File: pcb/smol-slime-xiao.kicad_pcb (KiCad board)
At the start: 4 copper layers, 20 x 23.5 mm, 11 parts, among them J2 Conn_01x02, U1 ICM-45686, U3 1532H, U4 XIAO-nRF52840-SMD

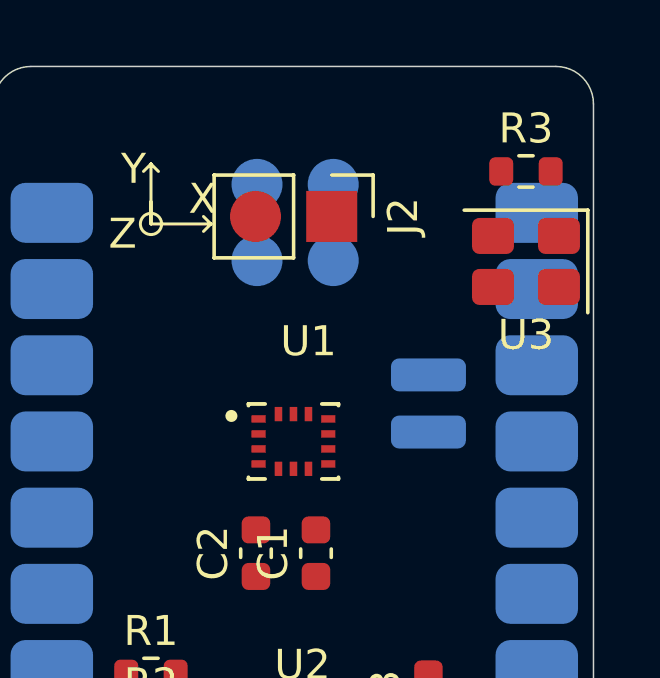
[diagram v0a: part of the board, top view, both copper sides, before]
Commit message: Add battery JST connector
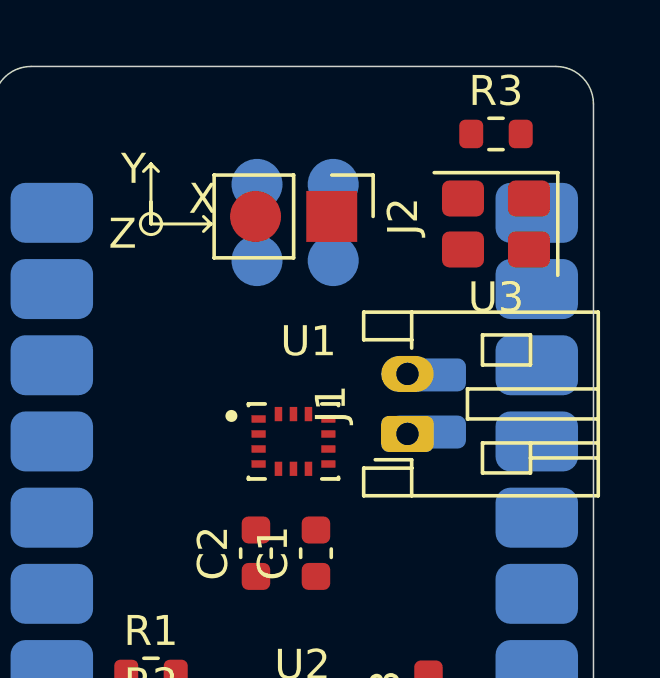
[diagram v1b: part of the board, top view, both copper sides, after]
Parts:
- added J1: Conn_01x02, Connector_JST:JST_PH_S2B-PH-K_1x02_P2.00mm_Horizontal, F.Cu at (153.8, 99.8)
- moved R3 1.60 mm to (156.8, 89.8)
- moved U3 1.60 mm to (156.8, 92.8)
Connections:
- J2 pad 1: GND -> +5V
- J2 pad 2: +5V -> GND

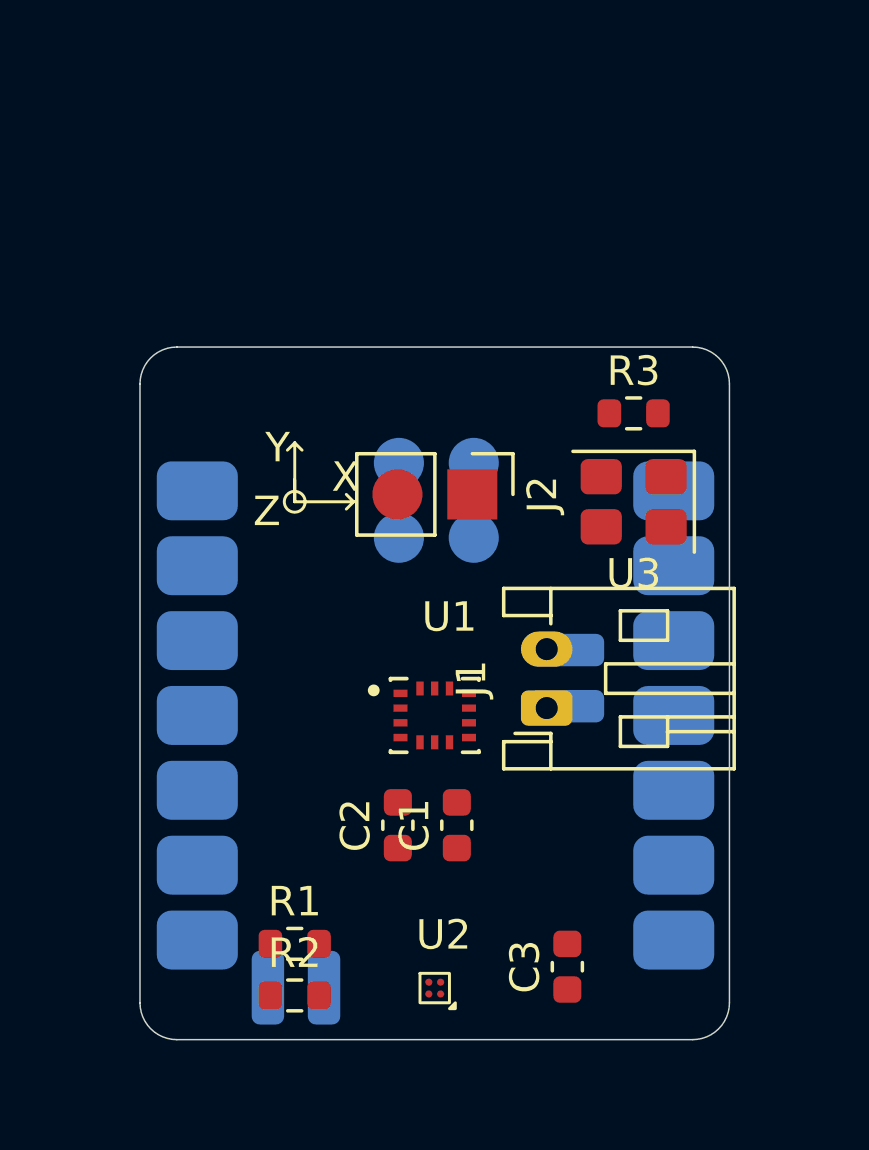
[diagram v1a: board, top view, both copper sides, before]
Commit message: Add descriptions to silkscreen
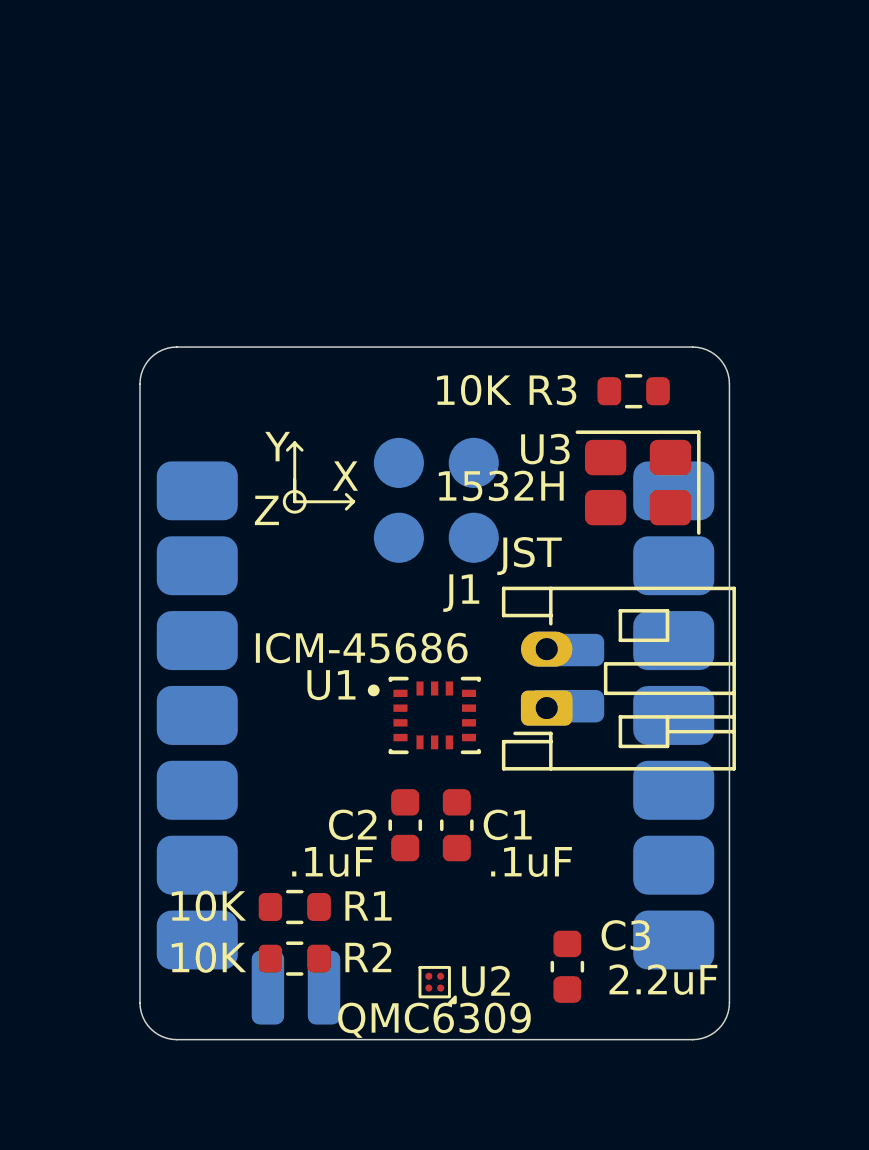
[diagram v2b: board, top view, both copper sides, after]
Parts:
- removed J2: Conn_01x02, Generic:PinPads_1x02_P2.54mm
- C1, C2: value 0.1uF -> .1uF
- J1: value Conn_01x02 -> JST
- U2: value ~ -> QMC6309
- moved R1 1.25 mm to (145.2, 106.5)
- moved R2 1.25 mm to (145.2, 108.2)
- moved R3 0.75 mm to (156.8, 89.0)
- moved U3 0.67 mm to (156.9, 92.1)
- moved C2 0.25 mm to (149.0, 103.7)
- moved U2 0.20 mm to (150.0, 109.0)

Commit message: Update pin pad footprint
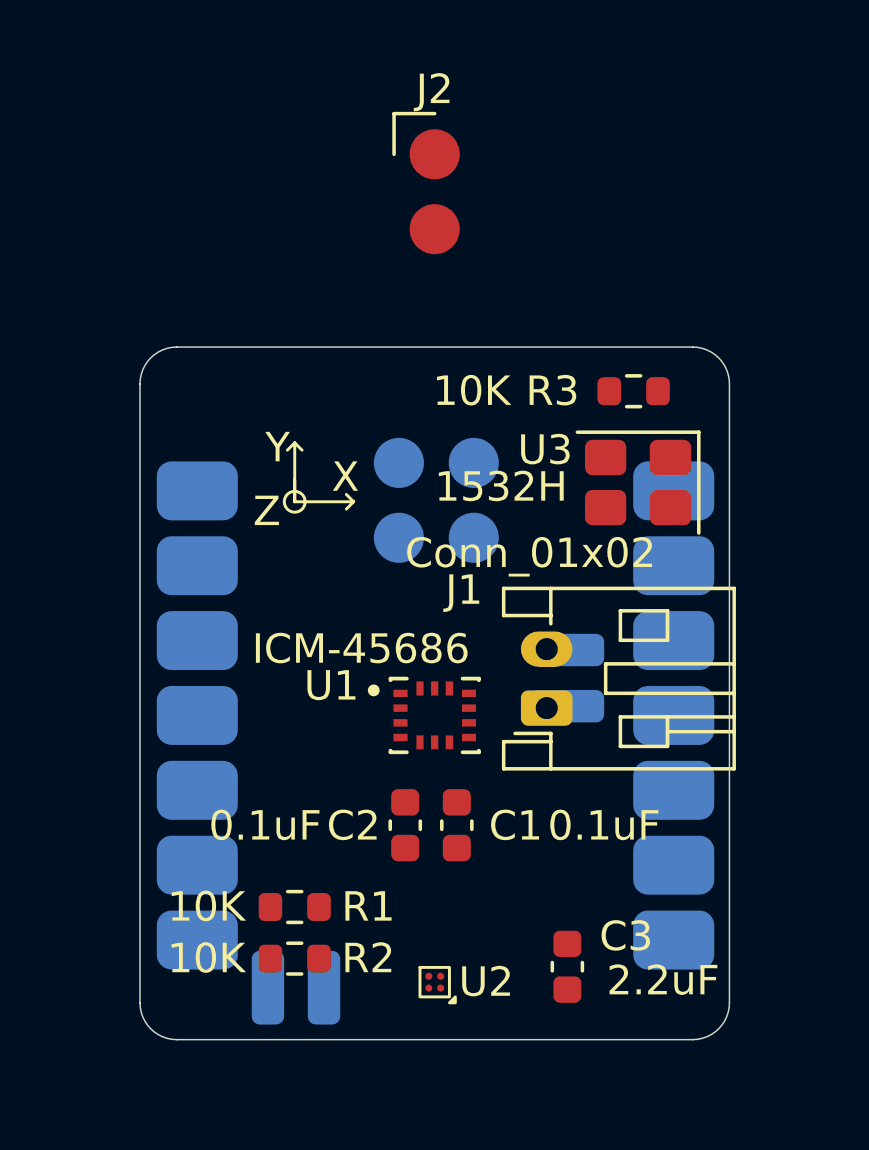
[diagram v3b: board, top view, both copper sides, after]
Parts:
- added J2: Conn_01x02, Generic:PinPads_1x02_P2.54mm, F.Cu at (150.0, 81.0)
- C1, C2: value .1uF -> 0.1uF
- J1: value JST -> Conn_01x02
- U2: value QMC6309 -> ~
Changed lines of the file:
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@@
 			)
 		)
-		(property "Value" "JST"
+		(property "Value" "Conn_01x02"
 			(at 5.25 -0.55 180)
 			(layer "F.SilkS")
@@
 			)
 		)
-		(property "Value" "QMC6309"
+		(property "Value" "~"
 			(at 0 1.25 0)
 			(unlocked yes)
@@
 		(tags "capacitor")
 		(property "Reference" "C1"
-			(at -0.025 1.75 180)
-			(layer "F.SilkS")
-			(effects
-				(font
-					(size 1 1)
-					(thickness 0.15)
-				)
-			)
-		)
-		(property "Value" ".1uF"
-			(at -1.275 2.5 180)
+			(at -0.025 2 180)
+			(layer "F.SilkS")
+			(effects
+				(font
+					(size 1 1)
+					(thickness 0.15)
+				)
+			)
+		)
+		(property "Value" "0.1uF"
+			(at -0.025 5 180)
 			(layer "F.SilkS")
 			(effects
@@
 			)
 		)
+	)
+	(footprint "Generic:PinPads_1x02_P2.54mm"
+		(layer "F.Cu")
+		(at 150 80.96)
+		(descr "Through hole straight pin header, 1x02, 2.54mm pitch, single row")
+		(tags "Through hole pin header THT 1x02 2.54mm single row")
+		(property "Reference" "J2"
+			(at 0 -2.2 0)
+			(layer "F.SilkS")
+			(effects
+				(font
+					(size 1 1)
+					(thickness 0.15)
+				)
+			)
+		)
+		(property "Value" "Conn_01x02"
+			(at 0 4.92 0)
+			(layer "F.Fab")
+			(hide yes)
+			(effects
+				(font
+					(size 1 1)
+					(thickness 0.15)
+				)
+			)
+		)
+		(property "Datasheet" "~"
+			(at 0 0 0)
+			(layer "F.Fab")
+			(hide yes)
+			(effects
+				(font
+					(size 1.27 1.27)
+					(thickness 0.15)
+				)
+			)
+		)
+		(property "Description" "Generic connector, single row, 01x02, script generated (kicad-library-utils/schlib/autogen/connector/)"
+			(at 0 0 0)
+			(layer "F.Fab")
+			(hide yes)
+			(effects
+				(font
+					(size 1.27 1.27)
+					(thickness 0.15)
+				)
+			)
+		)
+		(property ki_fp_filters "Connector*:*_1x??_*")
+		(sheetname "/")
+		(sheetfile "smol-slime-xiao.kicad_sch")
+		(attr through_hole)
+		(fp_line
+			(start -1.38 -1.38)
+			(end 0 -1.38)
+			(stroke
+				(width 0.12)
+				(type solid)
+			)
+			(layer "F.SilkS")
+		)
+		(fp_line
+			(start -1.38 0)
+			(end -1.38 -1.38)
+			(stroke
+				(width 0.12)
+				(type solid)
+			)
+			(layer "F.SilkS")
+		)
+		(fp_line
+			(start -1.5 -1.5)
+			(end -1.5 4)
+			(stroke
+				(width 0.05)
+				(type solid)
+			)
+			(layer "F.CrtYd")
+		)
+		(fp_line
+			(start -1.5 4)
+			(end 1.5 4)
+			(stroke
+				(width 0.05)
+				(type solid)
+			)
+			(layer "F.CrtYd")
+		)
+		(fp_line
+			(start 1.5 -1.5)
+			(end -1.5 -1.5)
+			(stroke
+				(width 0.05)
+				(type solid)
+			)
+			(layer "F.CrtYd")
+		)
+		(fp_line
+			(start 1.5 4)
+			(end 1.5 -1.5)
+			(stroke
+				(width 0.05)
+				(type solid)
+			)
+			(layer "F.CrtYd")
+		)
+		(fp_line
+			(start -1.27 -0.635)
+			(end -0.635 -1.27)
+			(stroke
+				(width 0.1)
+				(type solid)
+			)
+			(layer "F.Fab")
+		)
+		(fp_line
+			(start -1.27 3.81)
+			(end -1.27 -0.635)
+			(stroke
+				(width 0.1)
+				(type solid)
+			)
+			(layer "F.Fab")
+		)
+		(fp_line
+			(start -0.635 -1.27)
+			(end 1.27 -1.27)
+			(stroke
+				(width 0.1)
+				(type solid)
+			)
+			(layer "F.Fab")
+		)
+		(fp_line
+			(start 1.27 -1.27)
+			(end 1.27 3.81)
+			(stroke
+				(width 0.1)
+				(type solid)
+			)
+			(layer "F.Fab")
+		)
+		(fp_line
+			(start 1.27 3.81)
+			(end -1.27 3.81)
+			(stroke
+				(width 0.1)
+				(type solid)
+			)
+			(layer "F.Fab")
+		)
+		(fp_text user "${REFERENCE}"
+			(at 3 1.27 90)
+			(layer "F.Fab")
+			(effects
+				(font
+					(size 1 1)
+					(thickness 0.15)
+				)
+			)
+		)
+		(pad "1" smd circle
+			(at 0 0)
+			(size 1.7 1.7)
+			(layers "F.Cu" "F.Mask" "F.Paste")
+			(net 18 "+5V")
+			(pinfunction "Pin_1")
+			(pintype "passive")
+		)
+		(pad "2" smd circle
+			(at 0 2.54)
+			(size 1.7 1.7)
+			(layers "F.Cu" "F.Mask" "F.Paste")
+			(net 1 "GND")
+			(pinfunction "Pin_2")
+			(pintype "passive")
+		)
+		(embedded_fonts no)
 	)
 	(footprint "Capacitor_SMD:C_0603_1608Metric"
@@
 			)
 		)
-		(property "Value" ".1uF"
-			(at -1.275 -2.5 180)
-			(layer "F.SilkS")
-			(effects
+		(property "Value" "0.1uF"
+			(at -0.025 -4.75 180)
+			(layer "F.SilkS")
+			(effects

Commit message: Revert silkscreen verbosity
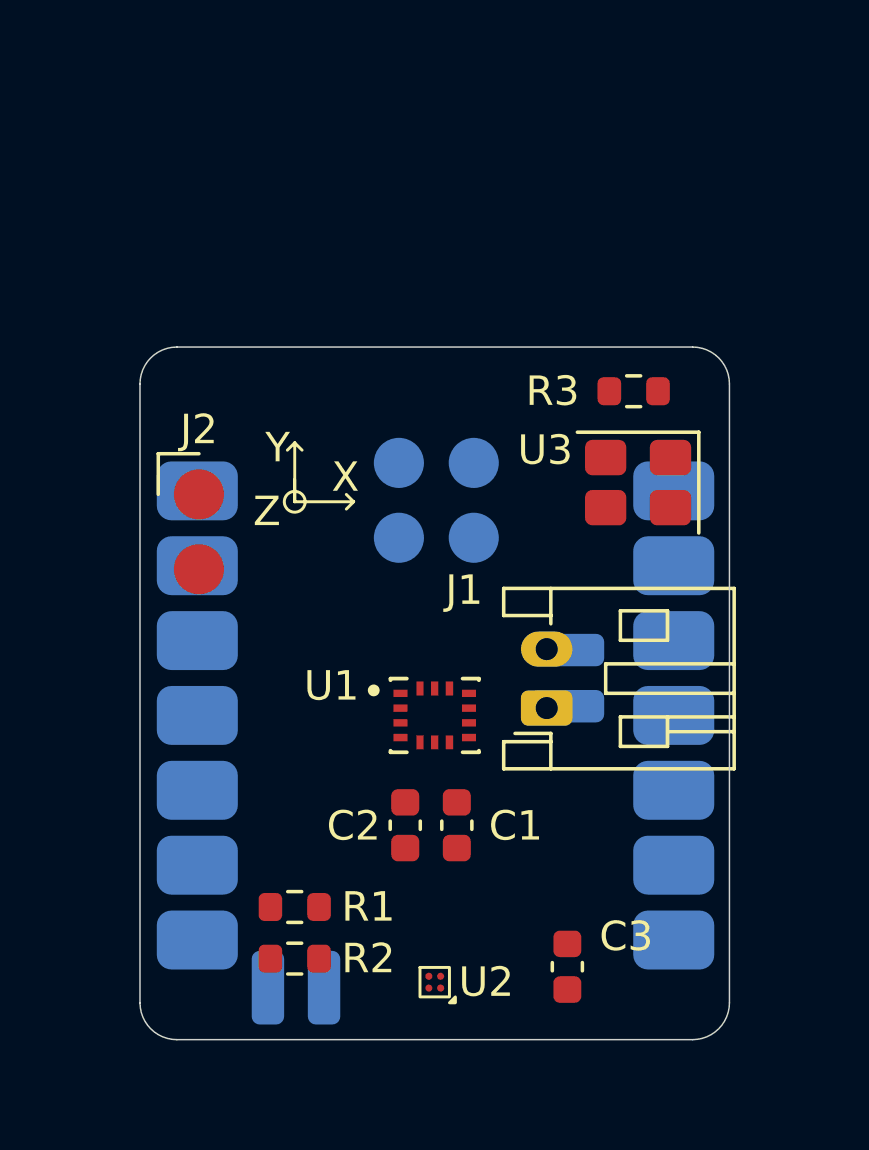
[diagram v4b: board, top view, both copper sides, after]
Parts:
- moved J2 14.0 mm to (142.0, 92.5)
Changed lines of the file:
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@@
 		(property "Value" "10K"
 			(at -5.5 0 0)
-			(layer "F.SilkS")
+			(layer "F.Fab")
 			(effects
 				(font
@@
 		(property "Value" "10K"
 			(at -3 0 0)
-			(layer "F.SilkS")
+			(layer "F.Fab")
 			(effects
 				(font
@@
 		(property "Value" "Conn_01x02"
 			(at 5.25 -0.55 180)
-			(layer "F.SilkS")
+			(layer "F.Fab")
 			(effects
 				(font
@@
 		(property "Value" "1532H"
 			(at 4.65 -0.15 0)
-			(layer "F.SilkS")
+			(layer "F.Fab")
 			(effects
 				(font
@@
 		(property "Value" "2.2uF"
 			(at -0.475 3.25 180)
-			(layer "F.SilkS")
+			(layer "F.Fab")
 			(effects
 				(font
@@
 		(property "Value" "10K"
 			(at -3 0 0)
-			(layer "F.SilkS")
+			(layer "F.Fab")
 			(effects
 				(font
@@
 		(property "Value" "0.1uF"
 			(at -0.025 5 180)
-			(layer "F.SilkS")
+			(layer "F.Fab")
 			(effects
 				(font
@@
 	(footprint "Generic:PinPads_1x02_P2.54mm"
 		(layer "F.Cu")
-		(at 150 80.96)
+		(at 142 92.5)
 		(descr "Through hole straight pin header, 1x02, 2.54mm pitch, single row")
 		(tags "Through hole pin header THT 1x02 2.54mm single row")
@@
 		(property "Value" "0.1uF"
 			(at -0.025 -4.75 180)
-			(layer "F.SilkS")
+			(layer "F.Fab")
 			(effects
 				(font
@@
 		(property "Value" "ICM-45686"
 			(at -2.5 -2.25 0)
-			(layer "F.SilkS")
-			(effects
-				(font
+			(layer "F.Fab")
+			(effects
+				(font

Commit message: Changed JST to SMT
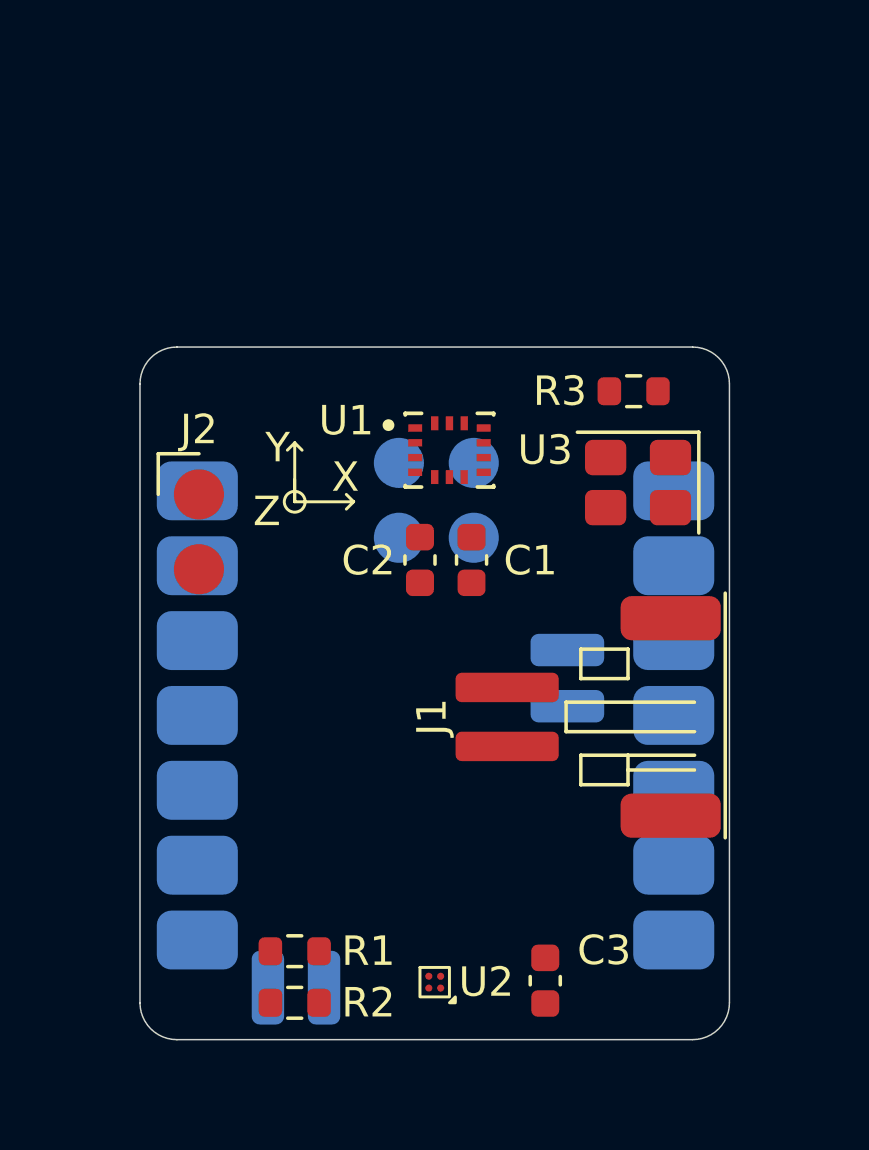
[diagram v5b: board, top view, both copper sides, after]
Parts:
- J1: footprint Connector_JST:JST_PH_S2B-PH-K_1x02_P2.00mm_Horizontal -> Generic:JST_PH2_SMT
- moved C1 9.01 mm to (151.2, 94.7)
- moved C2 9.01 mm to (149.5, 94.7)
- moved U1 9.01 mm to (150.5, 91.0)
- moved J1 1.87 mm to (152.5, 101.0)
- moved R1 1.50 mm to (145.2, 108.0)
- moved R2 1.50 mm to (145.2, 109.8)
- moved C3 0.89 mm to (153.8, 109.0)
